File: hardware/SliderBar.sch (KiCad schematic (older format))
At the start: 36 parts, among them J1 USB_B_Mini, J2 MOTOR_OUT, J3 POT_IN, J4 DEBUG, U1 MIC5205-3.3YM5, U2 TB6612FNG, U3 MT3608, U4 STM32F072C8Tx

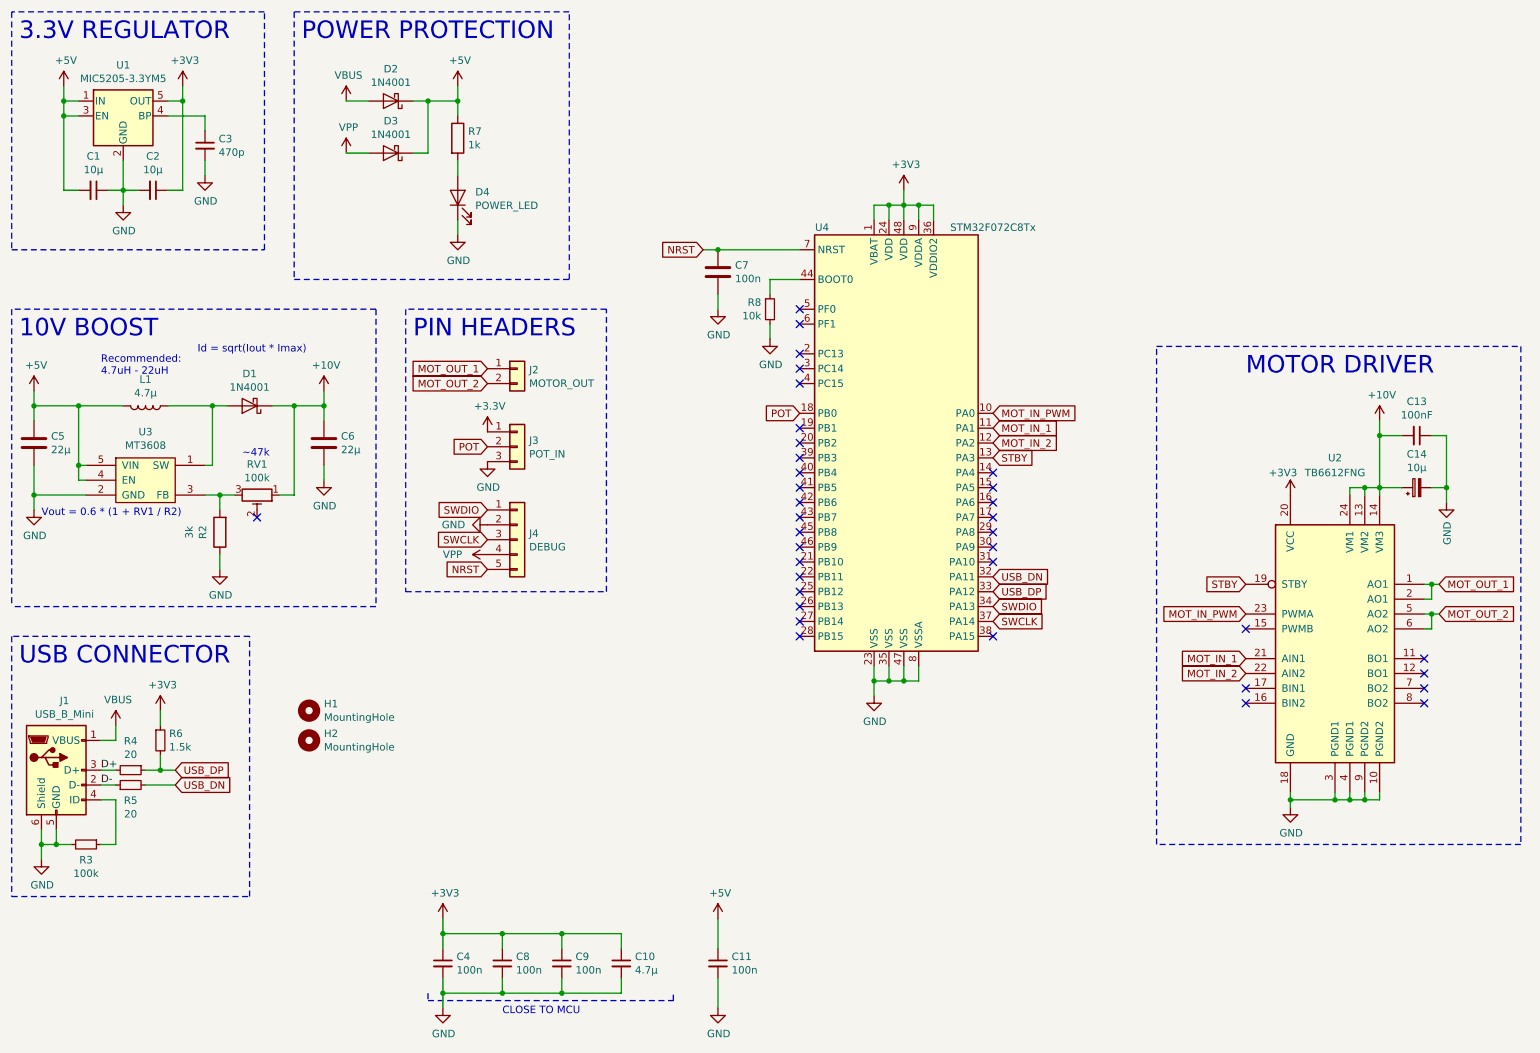
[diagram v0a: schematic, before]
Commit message: Move mounting holes to a schematic bloc
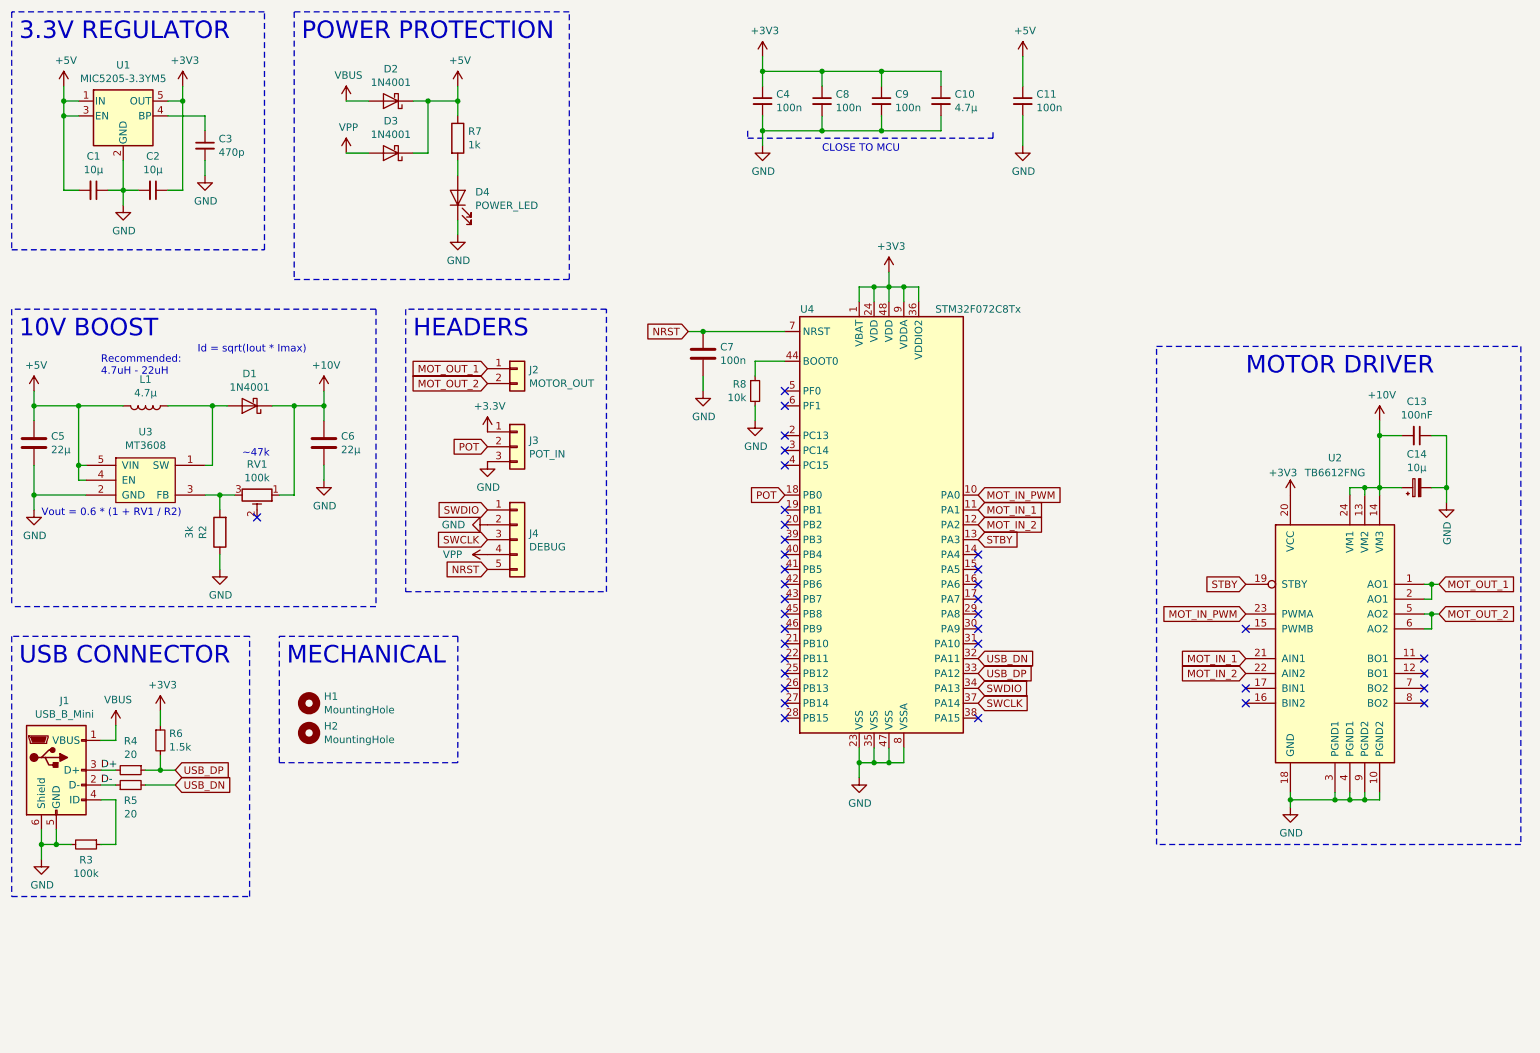
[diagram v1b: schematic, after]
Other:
- note added: "HEADERS"
- note added: "MECHANICAL"
- note removed: "PIN HEADERS"
- moved on the sheet: C10, C11, C4, C7, C8, C9, H1, H2, R8, U4

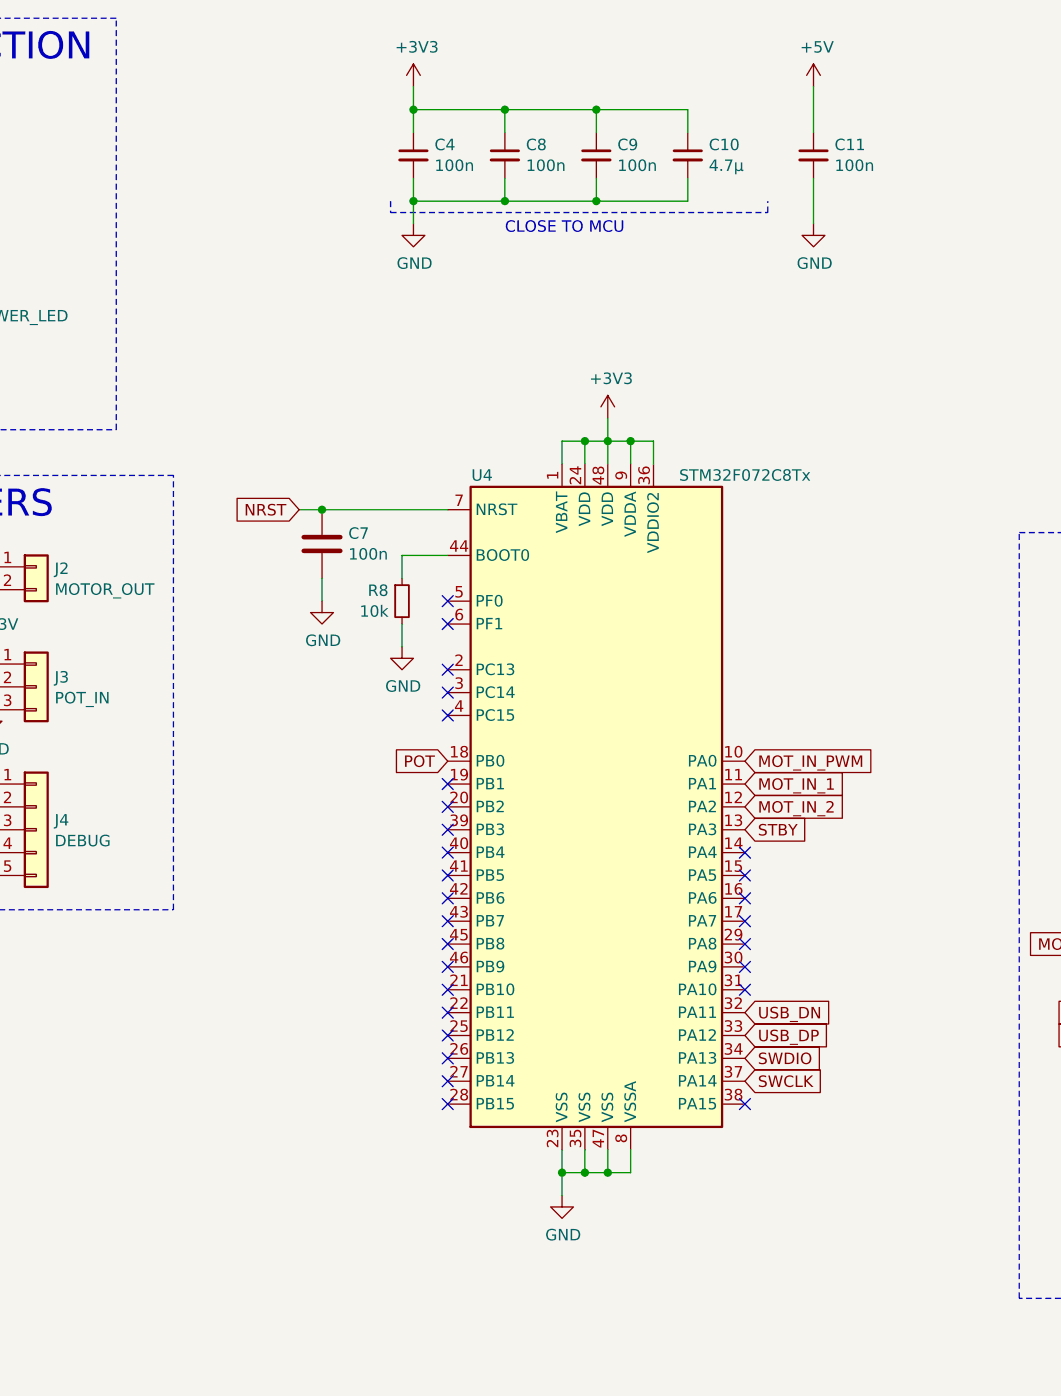
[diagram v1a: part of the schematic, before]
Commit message: Added DECOUPLING category to schematic
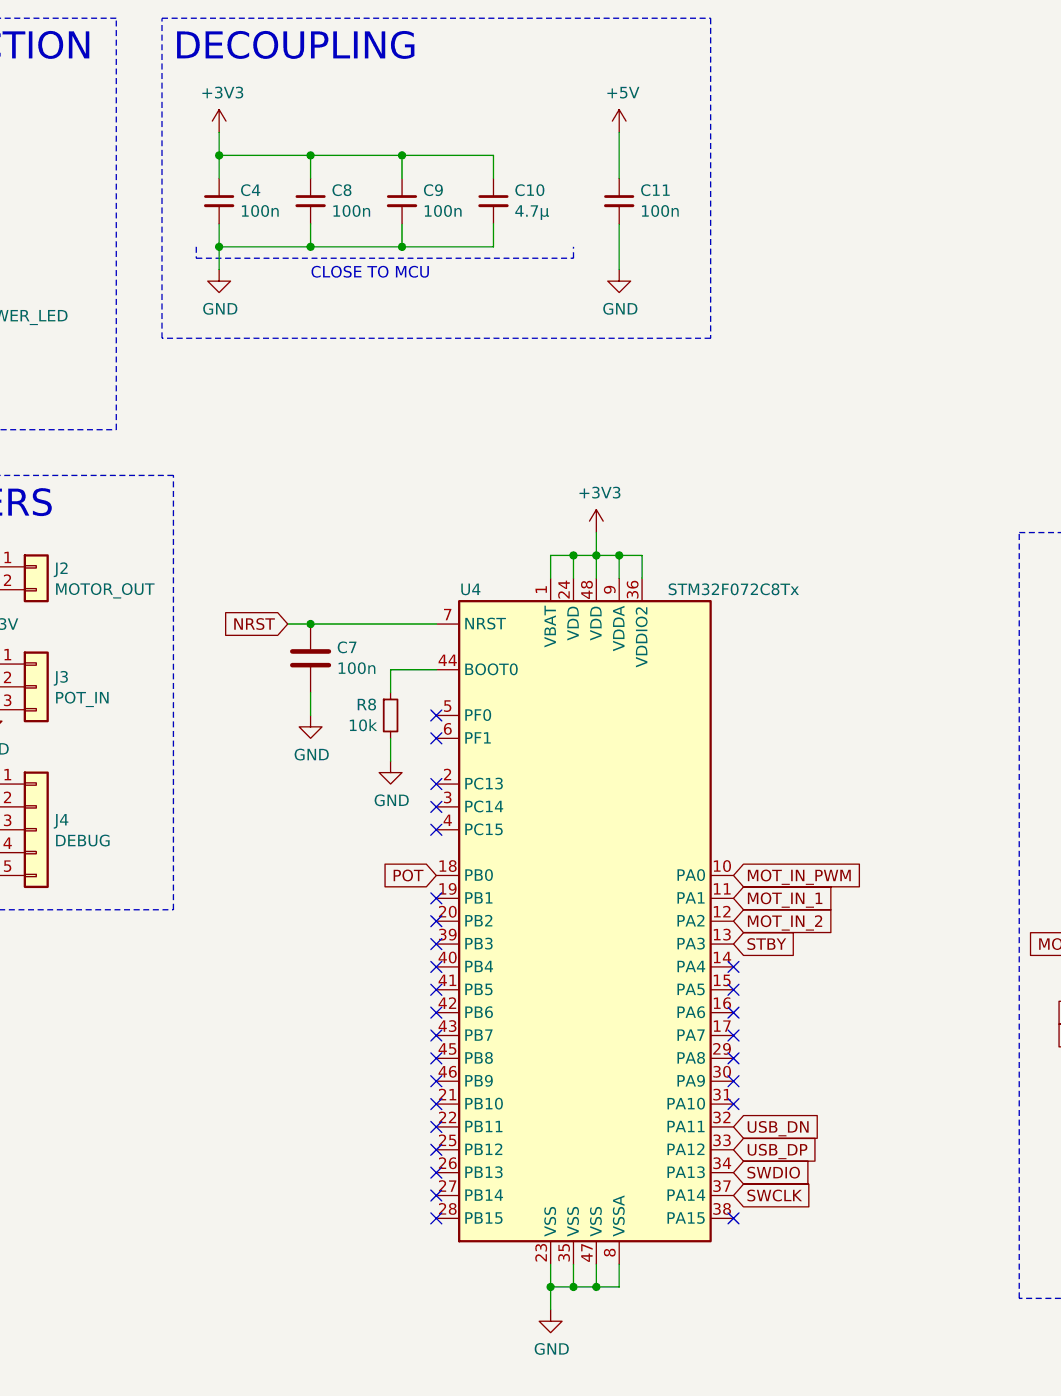
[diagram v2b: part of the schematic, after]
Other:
- note added: "DECOUPLING"
- moved on the sheet: C10, C11, C4, C7, C8, C9, R8, U4

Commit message: Final schematic update for prototype
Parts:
- renumbered C5 to C1, C13 to C12, C14 to C13, C1 to C2, C2 to C3, C3 to C4, C6 to C5, C4 to C6, C8 to C7, C7 to C8, R3 to R1, R4 to R2, R5 to R3, R6 to R4, R2 to R5, R7 to R6, R8 to R7, U3 to U2, U4 to U3, U2 to U4
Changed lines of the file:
@@
 $EndComp
 $Comp
-L Driver_Motor:TB6612FNG U2
+L Driver_Motor:TB6612FNG U4
 U 1 1 5BB2458F
 P 9650 4950
-F 0 "U2" H 9650 6200 50  0000 C CNN
+F 0 "U4" H 9650 6200 50  0000 C CNN
 F 1 "TB6612FNG" H 9650 6100 50  0000 C CNN
 F 2 "Package_SO:SSOP-24_5.3x8.2mm_P0.65mm" H 10100 5550 50  0001 C CNN
@@
 	6400 6250 6400 6150
 $Comp
-L MCU_ST_STM32F0:STM32F072C8Tx U4
+L MCU_ST_STM32F0:STM32F072C8Tx U3
 U 1 1 5BCADD80
 P 6600 4650
-F 0 "U4" H 6050 6100 50  0000 C CNN
+F 0 "U3" H 6050 6100 50  0000 C CNN
 F 1 "STM32F072C8Tx" H 7200 6100 50  0000 C CNN
 F 2 "Package_QFP:LQFP-48_7x7mm_P0.5mm" H 6000 3250 50  0001 R CNN
@@
 $EndComp
 $Comp
-L Device:C C7
+L Device:C C8
 U 1 1 5BCB759C
 P 5350 3500
-F 0 "C7" H 5465 3546 50  0000 L CNN
+F 0 "C8" H 5465 3546 50  0000 L CNN
 F 1 "100n" H 5465 3455 50  0000 L CNN
 F 2 "Capacitor_SMD:C_1206_3216Metric_Pad1.42x1.75mm_HandSolder" H 5388 3350 50  0001 C CNN
@@
 $EndComp
 $Comp
-L Device:C_Small C3
+L Device:C_Small C4
 U 1 1 5BD40CC0
 P 2050 1600
-F 0 "C3" H 2142 1646 50  0000 L CNN
+F 0 "C4" H 2142 1646 50  0000 L CNN
 F 1 "470p" H 2142 1555 50  0000 L CNN
 F 2 "Capacitor_SMD:C_1206_3216Metric_Pad1.42x1.75mm_HandSolder" H 2050 1600 50  0001 C CNN
@@
 	1400 1900 1500 1900
 $Comp
-L Device:C_Small C1
+L Device:C_Small C2
 U 1 1 5BD36320
 P 1300 1900
-F 0 "C1" V 1071 1900 50  0000 C CNN
+F 0 "C2" V 1071 1900 50  0000 C CNN
 F 1 "10µ" V 1162 1900 50  0000 C CNN
 F 2 "Capacitor_SMD:C_1206_3216Metric_Pad1.42x1.75mm_HandSolder" H 1300 1900 50  0001 C CNN
@@
 $EndComp
 $Comp
-L Device:C_Small C2
+L Device:C_Small C3
 U 1 1 5BD36275
 P 1700 1900
-F 0 "C2" V 1471 1900 50  0000 C CNN
+F 0 "C3" V 1471 1900 50  0000 C CNN
 F 1 "10µ" V 1562 1900 50  0000 C CNN
 F 2 "Capacitor_SMD:C_1206_3216Metric_Pad1.42x1.75mm_HandSolder" H 1700 1900 50  0001 C CNN
@@
 $EndComp
 $Comp
-L Device:C C6
+L Device:C C5
 U 1 1 5BC4B7C6
 P 2850 3600
-F 0 "C6" H 2735 3554 50  0000 R CNN
+F 0 "C5" H 2735 3554 50  0000 R CNN
 F 1 "22µ" H 2735 3645 50  0000 R CNN
 F 2 "Capacitor_SMD:C_1206_3216Metric_Pad1.42x1.75mm_HandSolder" H 2888 3450 50  0001 C CNN
@@
 $EndComp
 $Comp
-L Device:R R2
+L Device:R R5
 U 1 1 5BC47906
 P 2150 4200
-F 0 "R2" V 2265 4200 50  0000 C CNN
+F 0 "R5" V 2265 4200 50  0000 C CNN
 F 1 "3k" V 2356 4200 50  0000 C CNN
 F 2 "Resistor_SMD:R_1206_3216Metric_Pad1.42x1.75mm_HandSolder" V 2080 4200 50  0001 C CNN
@@
 $EndComp
 $Comp
-L Device:C C5
+L Device:C C1
 U 1 1 5BC3EFA6
 P 900 3600
-F 0 "C5" H 1015 3646 50  0000 L CNN
+F 0 "C1" H 1015 3646 50  0000 L CNN
 F 1 "22µ" H 1015 3555 50  0000 L CNN
 F 2 "Capacitor_SMD:C_1206_3216Metric_Pad1.42x1.75mm_HandSolder" H 938 3450 50  0001 C CNN
@@
 $EndComp
 $Comp
-L nelib:MT3608 U3
+L nelib:MT3608 U2
 U 1 1 5BC394FC
 P 1650 3850
-F 0 "U3" H 1650 4175 50  0000 C CNN
+F 0 "U2" H 1650 4175 50  0000 C CNN
 F 1 "MT3608" H 1650 4084 50  0000 C CNN
 F 2 "Package_TO_SOT_SMD:SOT-23-6_Handsoldering" H 1550 3200 50  0001 C CNN
@@
 STBY
 $Comp
-L Device:CP_Small C14
+L Device:CP_Small C13
 U 1 1 5BD914EE
 P 10200 3900
-F 0 "C14" V 10425 3900 50  0000 C CNN
+F 0 "C13" V 10425 3900 50  0000 C CNN
 F 1 "10µ" V 10334 3900 50  0000 C CNN
 F 2 "Capacitor_Tantalum_SMD:CP_EIA-7343-15_Kemet-W" H 10200 3900 50  0001 C CNN
@@
 $EndComp
 $Comp
-L Device:C_Small C13
+L Device:C_Small C12
 U 1 1 5BD9166F
 P 10200 3550
-F 0 "C13" V 9971 3550 50  0000 C CNN
+F 0 "C12" V 9971 3550 50  0000 C CNN
 F 1 "100nF" V 10062 3550 50  0000 C CNN
 F 2 "Capacitor_SMD:C_1206_3216Metric_Pad1.42x1.75mm_HandSolder" H 10200 3550 50  0001 C CNN
@@
 	3750 1300 3750 1200
 $Comp
-L Device:R R7
+L Device:R R6
 U 1 1 5BDBEFF0
 P 3750 1550
-F 0 "R7" H 3820 1596 50  0000 L CNN
+F 0 "R6" H 3820 1596 50  0000 L CNN
 F 1 "1k" H 3820 1505 50  0000 L CNN
 F 2 "Resistor_SMD:R_1206_3216Metric_Pad1.42x1.75mm_HandSolder" V 3680 1550 50  0001 C CNN
@@
 USB_DP
 $Comp
-L Device:R_Small R4
+L Device:R_Small R2
 U 1 1 5BDCCEB2
 P 1550 5800
-F 0 "R4" V 1354 5800 50  0000 C CNN
+F 0 "R2" V 1354 5800 50  0000 C CNN
 F 1 "20" V 1445 5800 50  0000 C CNN
 F 2 "Resistor_SMD:R_1206_3216Metric_Pad1.42x1.75mm_HandSolder" H 1550 5800 50  0001 C CNN
@@
 $EndComp
 $Comp
-L Device:R_Small R5
+L Device:R_Small R3
 U 1 1 5BDCCFBC
 P 1550 5900
-F 0 "R5" V 1446 5900 50  0000 C CNN
+F 0 "R3" V 1446 5900 50  0000 C CNN
 F 1 "20" V 1355 5900 50  0000 C CNN
 F 2 "Resistor_SMD:R_1206_3216Metric_Pad1.42x1.75mm_HandSolder" H 1550 5900 50  0001 C CNN
@@
 $EndComp
 $Comp
-L Device:R_Small R6
+L Device:R_Small R4
 U 1 1 5BDD3A19
 P 1750 5600
-F 0 "R6" H 1809 5646 50  0000 L CNN
+F 0 "R4" H 1809 5646 50  0000 L CNN
 F 1 "1.5k" H 1809 5555 50  0000 L CNN
 F 2 "Resistor_SMD:R_1206_3216Metric_Pad1.42x1.75mm_HandSolder" H 1750 5600 50  0001 C CNN
@@
 $EndComp
 $Comp
-L Device:R_Small R3
+L Device:R_Small R1
 U 1 1 5BDF23B7
 P 1250 6300
-F 0 "R3" V 1354 6300 50  0000 C CNN
+F 0 "R1" V 1354 6300 50  0000 C CNN
 F 1 "100k" V 1445 6300 50  0000 C CNN
 F 2 "Resistor_SMD:R_1206_3216Metric_Pad1.42x1.75mm_HandSolder" H 1250 6300 50  0001 C CNN
@@
 $EndComp
 $Comp
-L Device:C_Small C4
+L Device:C_Small C6
 U 1 1 5BE62B6A
 P 4950 1500
-F 0 "C4" H 5042 1546 50  0000 L CNN
+F 0 "C6" H 5042 1546 50  0000 L CNN
 F 1 "100n" H 5042 1455 50  0000 L CNN
 F 2 "Capacitor_SMD:C_1206_3216Metric_Pad1.42x1.75mm_HandSolder" H 4950 1500 50  0001 C CNN
@@
 $EndComp
 $Comp
-L Device:C_Small C8
+L Device:C_Small C7
 U 1 1 5BE68B0B
 P 5350 1500
-F 0 "C8" H 5442 1546 50  0000 L CNN
+F 0 "C7" H 5442 1546 50  0000 L CNN
 F 1 "100n" H 5442 1455 50  0000 L CNN
 F 2 "Capacitor_SMD:C_1206_3216Metric_Pad1.42x1.75mm_HandSolder" H 5350 1500 50  0001 C CNN
@@
 $EndComp
 $Comp
-L Device:R_Small R8
+L Device:R_Small R7
 U 1 1 5BEDBA2D
 P 5700 3750
-F 0 "R8" H 5641 3796 50  0000 R CNN
+F 0 "R7" H 5641 3796 50  0000 R CNN
 F 1 "10k" H 5641 3705 50  0000 R CNN
 F 2 "Resistor_SMD:R_1206_3216Metric_Pad1.42x1.75mm_HandSolder" H 5700 3750 50  0001 C CNN
